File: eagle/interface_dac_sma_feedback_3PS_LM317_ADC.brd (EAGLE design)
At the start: 112.3 x 143.4 mm, 41 parts, among them IC1 ISO1540, IC2 LT1352PA, IC3 LT1352PA, IC4 LM317MABDT, IC5 LM317MABDT, IC6 LM317MABDT, Q1 TIP122V, Q2 TIP122V, Q3 TIP122V, X1 BU-SMA-V

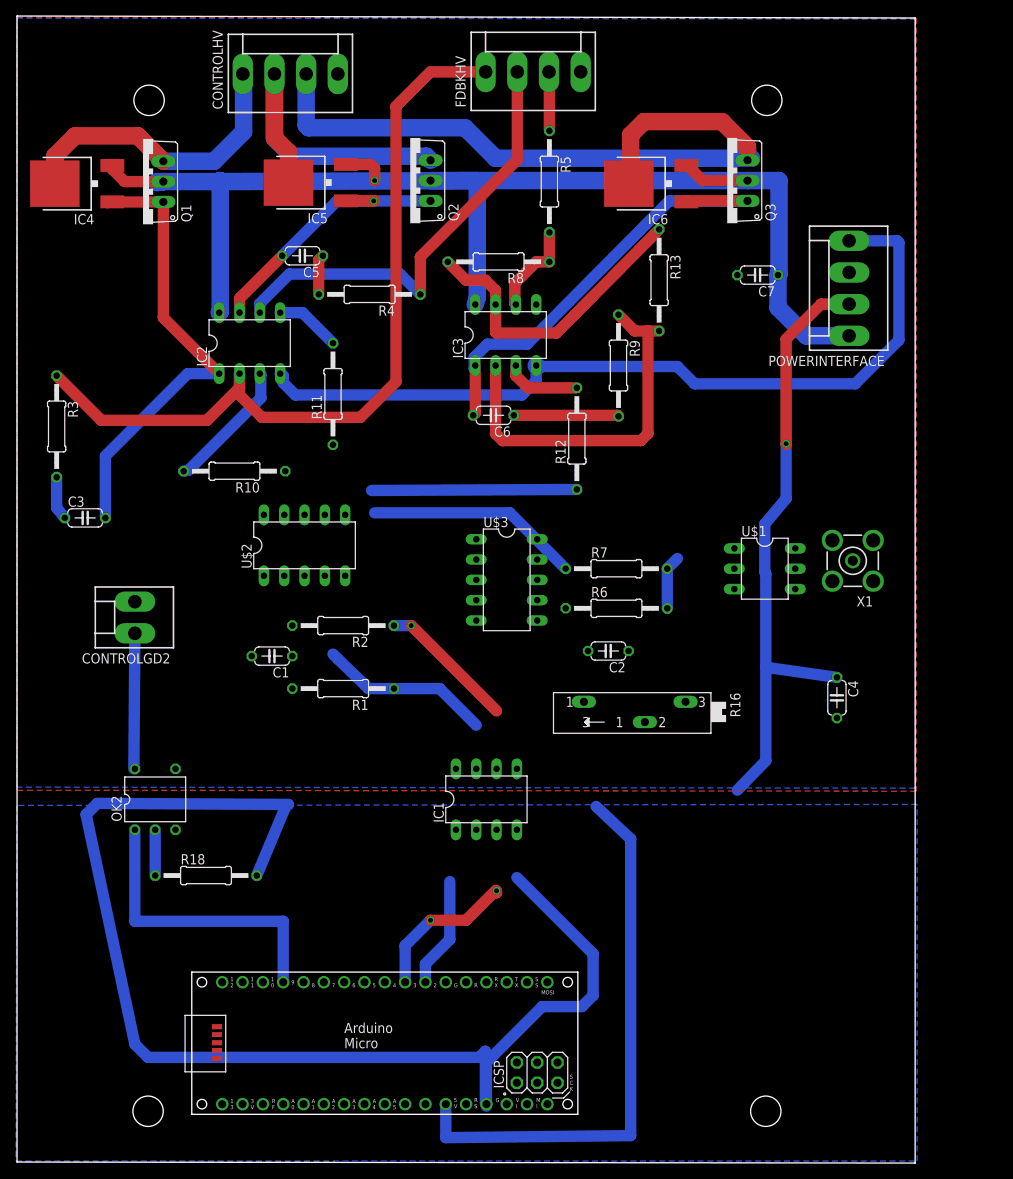
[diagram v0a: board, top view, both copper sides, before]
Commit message: Add adc
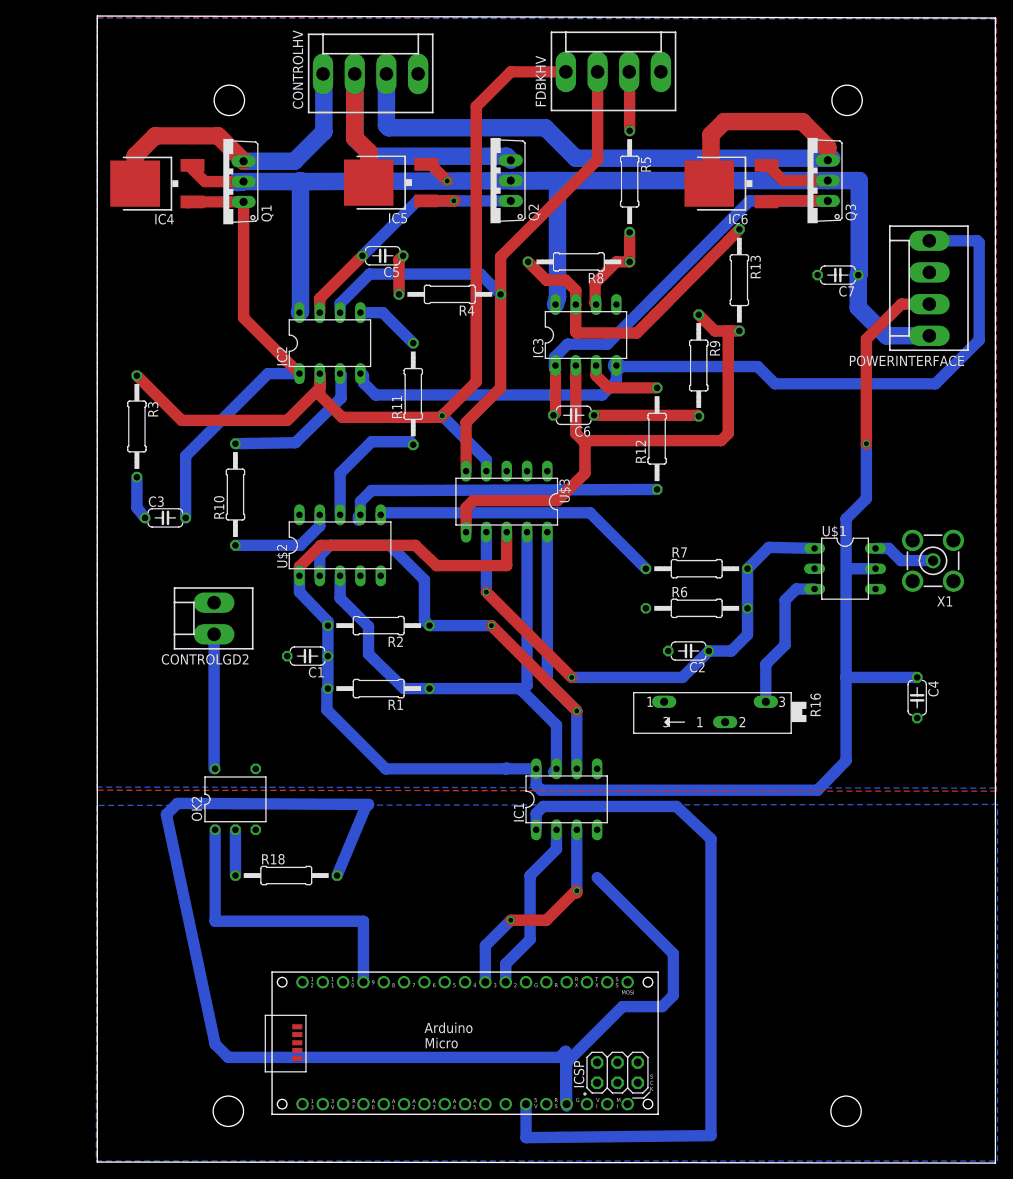
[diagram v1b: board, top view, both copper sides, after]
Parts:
- C1: value (none) -> 10n
- R16: value (none) -> 100k
- moved FDBKHV 10.0 mm to (64.5, 136.3)
- moved C2 10.0 mm to (73.9, 63.9)
- moved C3 10.0 mm to (8.51, 80.5)
- moved C4 10.0 mm to (102.5, 58.0)
- moved C6 10.0 mm to (59.6, 93.3)
- moved C7 10.0 mm to (92.6, 110.9)
- moved IC1 10.0 mm to (58.7, 45.3)
- moved IC3 10.0 mm to (61.1, 103.4)
- moved IC5 10.0 mm to (36.3, 122.4)
- moved IC6 10.0 mm to (78.9, 122.3)
- moved PCB1 10.0 mm to (21.8, 5.97)
- moved POWERINTERFACE 10.0 mm to (104.0, 109.2)
- moved Q2 10.0 mm to (49.1, 122.7)
- moved Q3 10.0 mm to (88.8, 122.7)
- moved R11 10.0 mm to (39.5, 96.0)
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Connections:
- removed net N$2: R6.2, R7.2
- net RDBK4: now also R6.2, R7.2
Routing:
- net VCC: track 77.5 -> 199.2 mm
- net RDBK4: track 0.00 -> 64.5 mm, vias 0 -> 2
- net SCL_OUT: track 17.2 -> 77.9 mm, vias 1 -> 2
- net SDA_OUT: track 21.6 -> 64.5 mm
- net RDBK2: track 56.6 -> 80.5 mm
- net RDBK3: track 47.0 -> 70.8 mm
- net A+5: track 70.3 -> 90.2 mm
- net N$12: track 0.00 -> 18.0 mm
- net N$26: track 0.00 -> 16.1 mm
- net N$25: track 25.7 -> 40.8 mm
- net N$24: track 0.00 -> 12.9 mm
- net N$1: track 26.8 -> 36.1 mm
- net RDBK1: track 101.3 -> 110.5 mm, vias 0 -> 1
- net SDA: track 13.8 -> 21.7 mm
- net SCL: track 19.3 -> 26.9 mm
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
